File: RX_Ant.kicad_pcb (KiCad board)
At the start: 2 copper layers, 100 x 100 mm, 44 parts, among them J1 CONN_COAXIAL, J10 CONN_COAXIAL, J11 CONN_01X06, J12 CONN_01X05, J13 CONN_COAXIAL, J14 CONN_COAXIAL, J15 CONN_COAXIAL, J16 CONN_01X01, J17 CONN_01X01, J18 CONN_01X01, J19 CONN_01X01, J2 CONN_COAXIAL, J20 CONN_01X01, J21 CONN_01X01, J22 CONN_01X01, J23 CONN_01X01, J3 CONN_COAXIAL, J4 CONN_COAXIAL, J5 CONN_COAXIAL, J6 CONN_COAXIAL, J7 CONN_COAXIAL, J8 CONN_COAXIAL, J9 CONN_COAXIAL

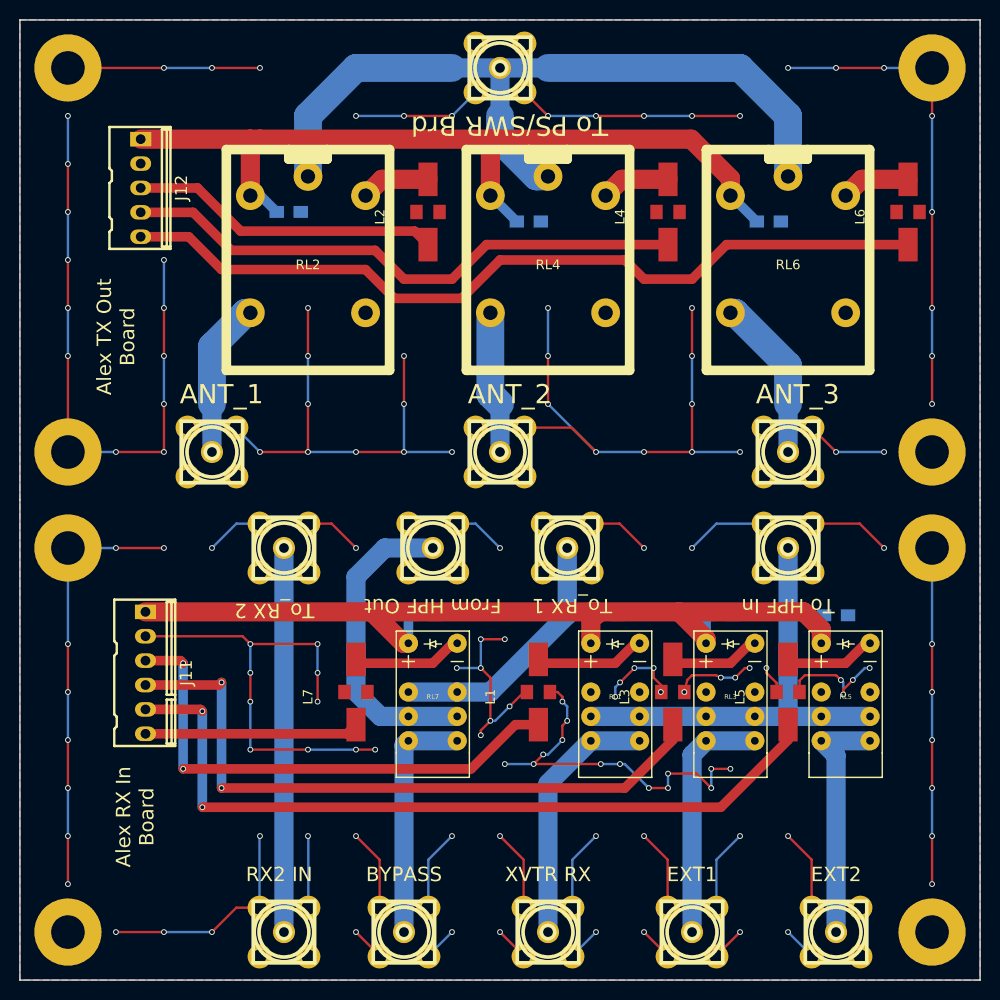
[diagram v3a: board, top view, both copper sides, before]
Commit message: few more vias added, tidying up some silkmask
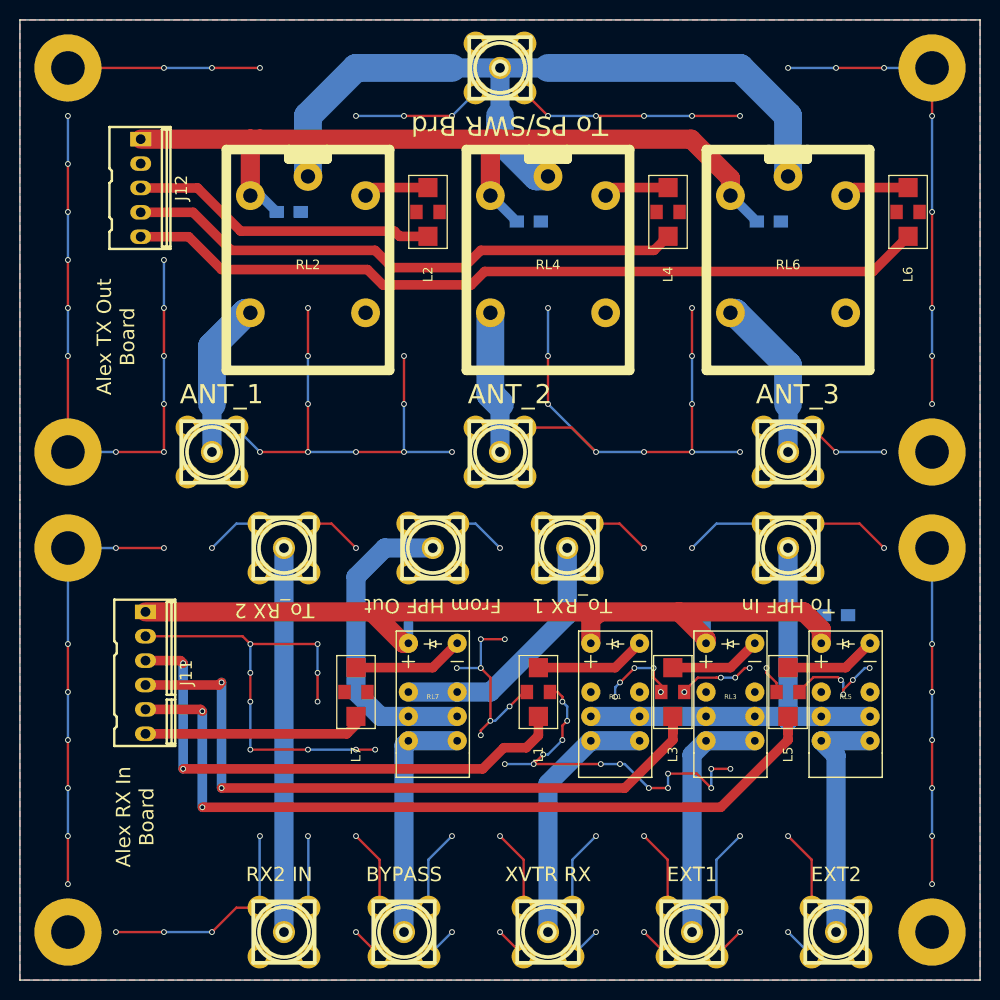
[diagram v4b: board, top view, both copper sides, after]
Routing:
- net Ant_3: track 86.6 -> 84.1 mm
- net RX3_IN: track 81.5 -> 83.2 mm
- net RX2_IN: track 69.7 -> 71.4 mm
- net Xvtr_IN: track 53.9 -> 55.5 mm
- net GND: track 661.1 -> 659.7 mm
- net Ant_2: track 59.3 -> 58.7 mm

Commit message: Gerber and BOM files added
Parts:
- added J24: CONN_COAXIAL, Connector_Coaxial:SMA_Amphenol_132289_EdgeMount, F.Cu at (47.4, 77.6)
- added J25: CONN_COAXIAL, Connector_Coaxial:SMA_Amphenol_132289_EdgeMount, F.Cu at (40.0, 72.4)
- added J26: CONN_COAXIAL, Connector_Coaxial:SMA_Amphenol_132289_EdgeMount, F.Cu at (75.0, 122.4)
- added J27: CONN_COAXIAL, Connector_Coaxial:SMA_Amphenol_132289_EdgeMount, F.Cu at (70.0, 72.4)
- added J28: CONN_COAXIAL, Connector_Coaxial:SMA_Amphenol_132289_EdgeMount, F.Cu at (100.0, 77.6)
- added J29: CONN_COAXIAL, Connector_Coaxial:SMA_Amphenol_132289_EdgeMount, F.Cu at (90.0, 122.4)
- added J30: CONN_COAXIAL, Connector_Coaxial:SMA_Amphenol_132289_EdgeMount, F.Cu at (100.0, 72.4)
- added J31: CONN_COAXIAL, Connector_Coaxial:SMA_Amphenol_132289_EdgeMount, F.Cu at (105.0, 122.4)
- added J32: CONN_COAXIAL, Connector_Coaxial:SMA_Amphenol_132289_EdgeMount, F.Cu at (60.0, 122.4)
- added J33: CONN_COAXIAL, Connector_Coaxial:SMA_Amphenol_132289_EdgeMount, F.Cu at (45.0, 122.4)
- added J34: CONN_COAXIAL, Connector_Coaxial:SMA_Amphenol_132289_EdgeMount, F.Cu at (70.0, 27.6)
- added J35: CONN_COAXIAL, Connector_Coaxial:SMA_Amphenol_132289_EdgeMount, F.Cu at (63.0, 77.6)
- added J36: CONN_COAXIAL, Connector_Coaxial:SMA_Amphenol_132289_EdgeMount, F.Cu at (78.0, 77.6)
- moved C9 5.23 mm to (62.6, 92.2)
- moved J13 2.50 mm to (45.0, 120.0)
- moved C5 2.00 mm to (83.0, 87.0)
- moved J7 1.00 mm to (78.0, 80.0)
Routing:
- net GND: track 659.7 -> 1060.8 mm, vias 137 -> 171
- net Net-(J34-Pad1): track 80.8 -> 71.0 mm
- net Net-(J13-Pad1): track 40.0 -> 45.9 mm
- net Net-(J36-Pad1): track 26.9 -> 29.7 mm
- net +12V: track 189.0 -> 186.4 mm
- net Net-(J32-Pad1): track 25.2 -> 27.6 mm
- net Net-(J31-Pad1): track 25.6 -> 28.0 mm
- net Net-(J29-Pad1): track 25.6 -> 28.0 mm
- net Net-(J28-Pad1): track 47.5 -> 49.9 mm
- net Net-(J27-Pad1): track 14.9 -> 17.3 mm
- net Net-(J2-Pad1): track 16.4 -> 18.8 mm
- net Net-(J10-Pad1): track 17.3 -> 19.7 mm
- net Net-(J1-Pad1): track 26.8 -> 29.2 mm
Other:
- board text added: "Ἀλεξιάρης"

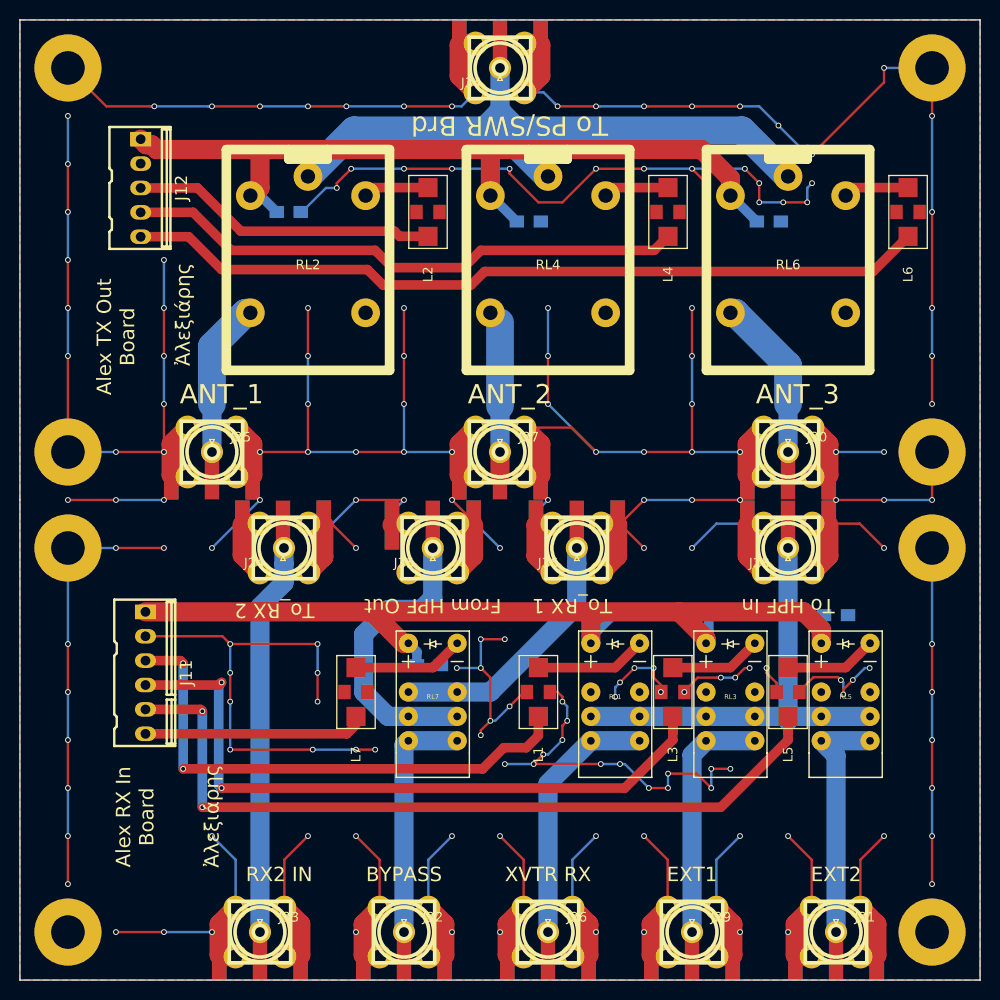
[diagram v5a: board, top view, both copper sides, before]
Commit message: via stitching added, new gerber
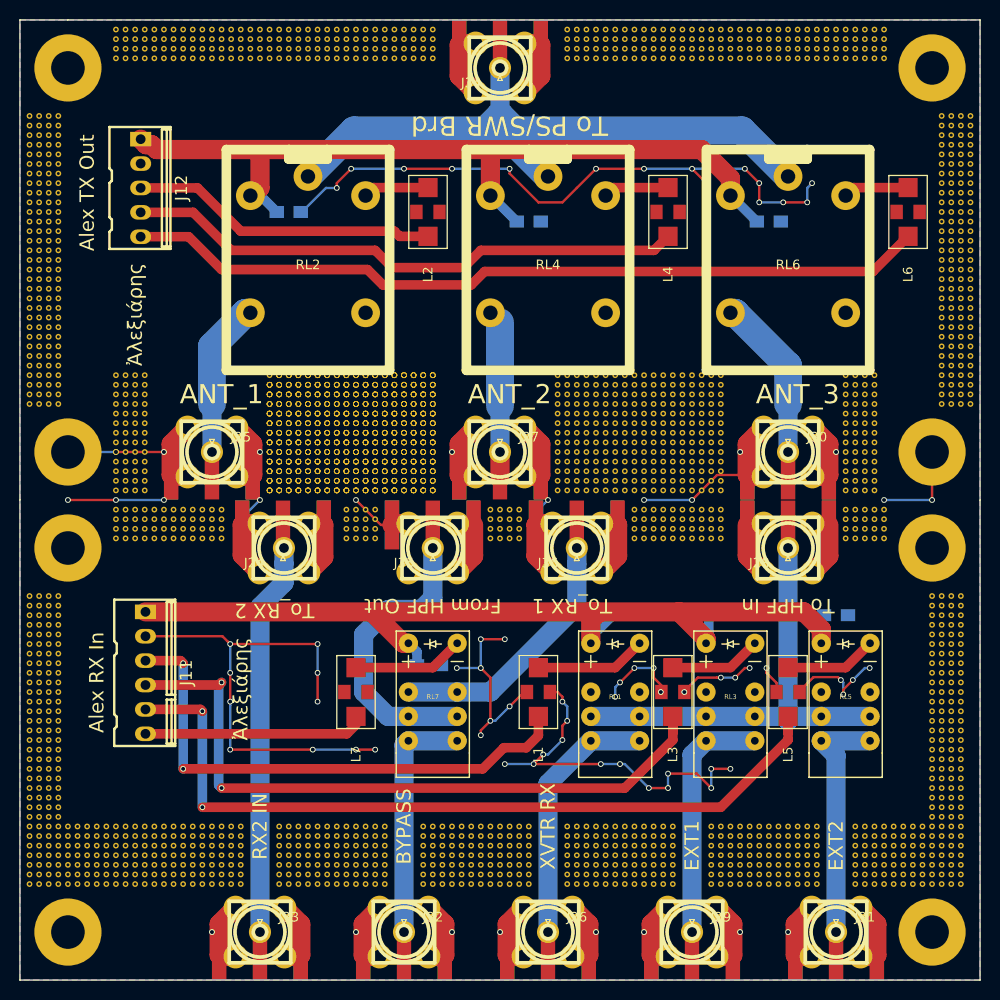
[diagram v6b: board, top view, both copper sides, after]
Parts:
- added REF**: via, via:via, F.Cu at (33.0, 74.0)
- added REF**: via, via:via, F.Cu at (32.0, 72.0)
- added REF**: via, via:via, F.Cu at (85.0, 77.0)
- added REF** (x3): via, via:via, F.Cu at (59.0, 71.0)
- added REF** (x3): via, via:via, F.Cu at (58.0, 71.0)
- added REF** (x3): via, via:via, F.Cu at (57.0, 71.0)
- added REF** (x3): via, via:via, F.Cu at (56.0, 71.0)
- added REF** (x3): via, via:via, F.Cu at (55.0, 71.0)
- added REF** (x3): via, via:via, F.Cu at (54.0, 71.0)
- added REF** (x3): via, via:via, F.Cu at (53.0, 71.0)
- added REF** (x3): via, via:via, F.Cu at (52.0, 71.0)
- added REF** (x3): via, via:via, F.Cu at (51.0, 71.0)
- added REF** (x3): via, via:via, F.Cu at (50.0, 71.0)
- added REF**: via, via:via, F.Cu at (84.0, 77.0)
- added REF** (x3): via, via:via, F.Cu at (49.0, 71.0)
- added REF** (x3): via, via:via, F.Cu at (48.0, 71.0)
- added REF** (x3): via, via:via, F.Cu at (47.0, 71.0)
- added REF** (x3): via, via:via, F.Cu at (46.0, 71.0)
- added REF** (x3): via, via:via, F.Cu at (63.0, 70.0)
- added REF** (x3): via, via:via, F.Cu at (62.0, 70.0)
- added REF** (x3): via, via:via, F.Cu at (61.0, 70.0)
- added REF** (x3): via, via:via, F.Cu at (60.0, 70.0)
- added REF** (x3): via, via:via, F.Cu at (59.0, 70.0)
- added REF** (x3): via, via:via, F.Cu at (58.0, 70.0)
- added REF**: via, via:via, F.Cu at (93.0, 76.0)
- added REF** (x3): via, via:via, F.Cu at (57.0, 70.0)
- added REF** (x3): via, via:via, F.Cu at (56.0, 70.0)
- added REF** (x3): via, via:via, F.Cu at (55.0, 70.0)
- added REF** (x3): via, via:via, F.Cu at (54.0, 70.0)
- added REF** (x3): via, via:via, F.Cu at (53.0, 70.0)
- added REF** (x3): via, via:via, F.Cu at (52.0, 70.0)
- added REF** (x3): via, via:via, F.Cu at (51.0, 70.0)
- added REF** (x3): via, via:via, F.Cu at (50.0, 70.0)
- added REF** (x3): via, via:via, F.Cu at (49.0, 70.0)
- added REF** (x3): via, via:via, F.Cu at (48.0, 70.0)
- added REF**: via, via:via, F.Cu at (92.0, 76.0)
- added REF** (x3): via, via:via, F.Cu at (47.0, 70.0)
- added REF** (x3): via, via:via, F.Cu at (46.0, 70.0)
- added REF** (x3): via, via:via, F.Cu at (63.0, 69.0)
- added REF** (x3): via, via:via, F.Cu at (62.0, 69.0)
- added REF** (x3): via, via:via, F.Cu at (61.0, 69.0)
- added REF** (x3): via, via:via, F.Cu at (60.0, 69.0)
- added REF** (x3): via, via:via, F.Cu at (59.0, 69.0)
- added REF** (x3): via, via:via, F.Cu at (58.0, 69.0)
- added REF** (x3): via, via:via, F.Cu at (57.0, 69.0)
- added REF** (x3): via, via:via, F.Cu at (56.0, 69.0)
- added REF**: via, via:via, F.Cu at (91.0, 76.0)
- added REF** (x3): via, via:via, F.Cu at (55.0, 69.0)
- added REF** (x3): via, via:via, F.Cu at (54.0, 69.0)
- added REF** (x3): via, via:via, F.Cu at (53.0, 69.0)
- added REF** (x3): via, via:via, F.Cu at (52.0, 69.0)
- added REF** (x3): via, via:via, F.Cu at (51.0, 69.0)
- added REF** (x3): via, via:via, F.Cu at (50.0, 69.0)
- added REF** (x3): via, via:via, F.Cu at (49.0, 69.0)
- added REF** (x3): via, via:via, F.Cu at (48.0, 69.0)
- added REF** (x3): via, via:via, F.Cu at (47.0, 69.0)
- added REF** (x3): via, via:via, F.Cu at (46.0, 69.0)
- added REF**: via, via:via, F.Cu at (90.0, 76.0)
- added REF** (x3): via, via:via, F.Cu at (63.0, 68.0)
- added REF** (x3): via, via:via, F.Cu at (62.0, 68.0)
- added REF** (x3): via, via:via, F.Cu at (61.0, 68.0)
- added REF** (x3): via, via:via, F.Cu at (60.0, 68.0)
- added REF** (x3): via, via:via, F.Cu at (59.0, 68.0)
- added REF** (x3): via, via:via, F.Cu at (58.0, 68.0)
- added REF** (x3): via, via:via, F.Cu at (57.0, 68.0)
- added REF** (x3): via, via:via, F.Cu at (56.0, 68.0)
- added REF** (x3): via, via:via, F.Cu at (55.0, 68.0)
- added REF** (x3): via, via:via, F.Cu at (54.0, 68.0)
- added REF**: via, via:via, F.Cu at (89.0, 76.0)
- added REF** (x3): via, via:via, F.Cu at (53.0, 68.0)
- added REF** (x3): via, via:via, F.Cu at (52.0, 68.0)
- added REF** (x3): via, via:via, F.Cu at (51.0, 68.0)
- added REF** (x3): via, via:via, F.Cu at (50.0, 68.0)
- added REF** (x3): via, via:via, F.Cu at (49.0, 68.0)
- added REF** (x3): via, via:via, F.Cu at (48.0, 68.0)
- added REF** (x3): via, via:via, F.Cu at (47.0, 68.0)
- added REF** (x3): via, via:via, F.Cu at (46.0, 68.0)
- added REF** (x3): via, via:via, F.Cu at (63.0, 67.0)
- added REF** (x3): via, via:via, F.Cu at (62.0, 67.0)
- added REF**: via, via:via, F.Cu at (88.0, 76.0)
- added REF** (x3): via, via:via, F.Cu at (61.0, 67.0)
- added REF** (x3): via, via:via, F.Cu at (60.0, 67.0)
- added REF** (x3): via, via:via, F.Cu at (59.0, 67.0)
- added REF** (x3): via, via:via, F.Cu at (58.0, 67.0)
- added REF** (x3): via, via:via, F.Cu at (57.0, 67.0)
- added REF** (x3): via, via:via, F.Cu at (56.0, 67.0)
- added REF** (x3): via, via:via, F.Cu at (55.0, 67.0)
- added REF** (x3): via, via:via, F.Cu at (54.0, 67.0)
- added REF** (x3): via, via:via, F.Cu at (53.0, 67.0)
- added REF** (x3): via, via:via, F.Cu at (52.0, 67.0)
- added REF**: via, via:via, F.Cu at (87.0, 76.0)
- added REF** (x3): via, via:via, F.Cu at (51.0, 67.0)
- added REF** (x3): via, via:via, F.Cu at (50.0, 67.0)
- added REF** (x3): via, via:via, F.Cu at (49.0, 67.0)
- added REF** (x3): via, via:via, F.Cu at (48.0, 67.0)
- added REF** (x3): via, via:via, F.Cu at (47.0, 67.0)
- added REF** (x3): via, via:via, F.Cu at (46.0, 67.0)
- added REF** (x3): via, via:via, F.Cu at (63.0, 66.0)
- added REF** (x3): via, via:via, F.Cu at (62.0, 66.0)
- added REF** (x3): via, via:via, F.Cu at (61.0, 66.0)
- added REF** (x3): via, via:via, F.Cu at (60.0, 66.0)
- added REF**: via, via:via, F.Cu at (86.0, 76.0)
- added REF** (x3): via, via:via, F.Cu at (59.0, 66.0)
- added REF** (x3): via, via:via, F.Cu at (58.0, 66.0)
- added REF** (x3): via, via:via, F.Cu at (57.0, 66.0)
- added REF** (x3): via, via:via, F.Cu at (56.0, 66.0)
- added REF** (x3): via, via:via, F.Cu at (55.0, 66.0)
- added REF** (x3): via, via:via, F.Cu at (54.0, 66.0)
- added REF** (x3): via, via:via, F.Cu at (53.0, 66.0)
- added REF** (x3): via, via:via, F.Cu at (52.0, 66.0)
- added REF** (x3): via, via:via, F.Cu at (51.0, 66.0)
- added REF** (x3): via, via:via, F.Cu at (50.0, 66.0)
- added REF**: via, via:via, F.Cu at (31.0, 72.0)
- added REF**: via, via:via, F.Cu at (85.0, 76.0)
- added REF** (x3): via, via:via, F.Cu at (49.0, 66.0)
- added REF** (x3): via, via:via, F.Cu at (48.0, 66.0)
- added REF** (x3): via, via:via, F.Cu at (47.0, 66.0)
- added REF** (x3): via, via:via, F.Cu at (46.0, 66.0)
- added REF** (x3): via, via:via, F.Cu at (63.0, 65.0)
- added REF** (x3): via, via:via, F.Cu at (62.0, 65.0)
- added REF** (x3): via, via:via, F.Cu at (61.0, 65.0)
- added REF** (x3): via, via:via, F.Cu at (60.0, 65.0)
- added REF** (x3): via, via:via, F.Cu at (59.0, 65.0)
- added REF** (x3): via, via:via, F.Cu at (58.0, 65.0)
- added REF**: via, via:via, F.Cu at (84.0, 76.0)
- added REF** (x3): via, via:via, F.Cu at (57.0, 65.0)
- added REF** (x3): via, via:via, F.Cu at (56.0, 65.0)
- added REF** (x3): via, via:via, F.Cu at (55.0, 65.0)
- added REF** (x3): via, via:via, F.Cu at (54.0, 65.0)
- added REF** (x3): via, via:via, F.Cu at (53.0, 65.0)
- added REF** (x3): via, via:via, F.Cu at (52.0, 65.0)
- added REF** (x3): via, via:via, F.Cu at (51.0, 65.0)
- added REF** (x3): via, via:via, F.Cu at (50.0, 65.0)
- added REF** (x3): via, via:via, F.Cu at (49.0, 65.0)
- added REF** (x3): via, via:via, F.Cu at (48.0, 65.0)
- added REF**: via, via:via, F.Cu at (72.0, 79.0)
- added REF** (x3): via, via:via, F.Cu at (47.0, 65.0)
- added REF** (x3): via, via:via, F.Cu at (46.0, 65.0)
- added REF** (x3): via, via:via, F.Cu at (63.0, 64.0)
- added REF** (x3): via, via:via, F.Cu at (62.0, 64.0)
- added REF** (x3): via, via:via, F.Cu at (61.0, 64.0)
- added REF** (x3): via, via:via, F.Cu at (60.0, 64.0)
- added REF** (x3): via, via:via, F.Cu at (59.0, 64.0)
- added REF** (x3): via, via:via, F.Cu at (58.0, 64.0)
- added REF** (x3): via, via:via, F.Cu at (57.0, 64.0)
- added REF** (x3): via, via:via, F.Cu at (56.0, 64.0)
- added REF**: via, via:via, F.Cu at (71.0, 79.0)
- added REF** (x3): via, via:via, F.Cu at (55.0, 64.0)
- added REF** (x3): via, via:via, F.Cu at (54.0, 64.0)
- added REF** (x3): via, via:via, F.Cu at (53.0, 64.0)
- added REF** (x3): via, via:via, F.Cu at (52.0, 64.0)
- added REF** (x3): via, via:via, F.Cu at (51.0, 64.0)
- added REF** (x3): via, via:via, F.Cu at (50.0, 64.0)
- added REF** (x3): via, via:via, F.Cu at (49.0, 64.0)
- added REF** (x3): via, via:via, F.Cu at (48.0, 64.0)
- added REF** (x3): via, via:via, F.Cu at (47.0, 64.0)
- added REF** (x3): via, via:via, F.Cu at (46.0, 64.0)
- added REF**: via, via:via, F.Cu at (70.0, 79.0)
- added REF** (x3): via, via:via, F.Cu at (63.0, 63.0)
- added REF** (x3): via, via:via, F.Cu at (62.0, 63.0)
- added REF** (x3): via, via:via, F.Cu at (61.0, 63.0)
- added REF** (x3): via, via:via, F.Cu at (60.0, 63.0)
- added REF** (x3): via, via:via, F.Cu at (59.0, 63.0)
- added REF** (x3): via, via:via, F.Cu at (58.0, 63.0)
- added REF** (x3): via, via:via, F.Cu at (57.0, 63.0)
- added REF** (x3): via, via:via, F.Cu at (56.0, 63.0)
- added REF** (x3): via, via:via, F.Cu at (55.0, 63.0)
- added REF** (x3): via, via:via, F.Cu at (54.0, 63.0)
- added REF**: via, via:via, F.Cu at (69.0, 79.0)
- added REF** (x3): via, via:via, F.Cu at (53.0, 63.0)
- added REF** (x3): via, via:via, F.Cu at (52.0, 63.0)
- added REF** (x3): via, via:via, F.Cu at (51.0, 63.0)
- added REF** (x3): via, via:via, F.Cu at (50.0, 63.0)
- added REF** (x3): via, via:via, F.Cu at (49.0, 63.0)
- added REF** (x3): via, via:via, F.Cu at (48.0, 63.0)
- added REF** (x3): via, via:via, F.Cu at (47.0, 63.0)
- added REF** (x3): via, via:via, F.Cu at (46.0, 63.0)
- added REF** (x3): via, via:via, F.Cu at (63.0, 62.0)
- added REF** (x3): via, via:via, F.Cu at (62.0, 62.0)
- added REF**: via, via:via, F.Cu at (72.0, 78.0)
- added REF** (x3): via, via:via, F.Cu at (61.0, 62.0)
- added REF** (x3): via, via:via, F.Cu at (60.0, 62.0)
- added REF** (x3): via, via:via, F.Cu at (59.0, 62.0)
- added REF** (x3): via, via:via, F.Cu at (58.0, 62.0)
- added REF** (x3): via, via:via, F.Cu at (57.0, 62.0)
- added REF** (x3): via, via:via, F.Cu at (56.0, 62.0)
- added REF** (x3): via, via:via, F.Cu at (55.0, 62.0)
- added REF** (x3): via, via:via, F.Cu at (54.0, 62.0)
- added REF** (x3): via, via:via, F.Cu at (53.0, 62.0)
- added REF** (x3): via, via:via, F.Cu at (52.0, 62.0)
- added REF**: via, via:via, F.Cu at (71.0, 78.0)
- added REF** (x3): via, via:via, F.Cu at (51.0, 62.0)
- added REF** (x3): via, via:via, F.Cu at (50.0, 62.0)
- added REF** (x3): via, via:via, F.Cu at (49.0, 62.0)
- added REF** (x3): via, via:via, F.Cu at (48.0, 62.0)
- added REF** (x3): via, via:via, F.Cu at (47.0, 62.0)
- added REF**: via, via:via, F.Cu at (76.0, 62.0)
- added REF**: via, via:via, F.Cu at (46.0, 62.0)
- added REF**: via, via:via, F.Cu at (30.0, 62.0)
- added REF**: via, via:via, F.Cu at (114.0, 115.0)
- added REF**: via, via:via, F.Cu at (113.0, 115.0)
- added REF**: via, via:via, F.Cu at (70.0, 78.0)
- added REF**: via, via:via, F.Cu at (112.0, 115.0)
- added REF**: via, via:via, F.Cu at (111.0, 115.0)
- added REF**: via, via:via, F.Cu at (110.0, 115.0)
- added REF**: via, via:via, F.Cu at (109.0, 115.0)
- added REF**: via, via:via, F.Cu at (108.0, 115.0)
- added REF**: via, via:via, F.Cu at (107.0, 115.0)
- added REF**: via, via:via, F.Cu at (114.0, 114.0)
- added REF**: via, via:via, F.Cu at (113.0, 114.0)
- added REF**: via, via:via, F.Cu at (112.0, 114.0)
- added REF**: via, via:via, F.Cu at (111.0, 114.0)
- added REF**: via, via:via, F.Cu at (69.0, 78.0)
- added REF**: via, via:via, F.Cu at (110.0, 114.0)
- added REF**: via, via:via, F.Cu at (109.0, 114.0)
- added REF**: via, via:via, F.Cu at (108.0, 114.0)
- added REF**: via, via:via, F.Cu at (107.0, 114.0)
- added REF**: via, via:via, F.Cu at (114.0, 113.0)
- added REF**: via, via:via, F.Cu at (113.0, 113.0)
- added REF**: via, via:via, F.Cu at (112.0, 113.0)
- added REF**: via, via:via, F.Cu at (111.0, 113.0)
- added REF**: via, via:via, F.Cu at (110.0, 113.0)
- added REF**: via, via:via, F.Cu at (109.0, 113.0)
- added REF**: via, via:via, F.Cu at (30.0, 72.0)
- added REF**: via, via:via, F.Cu at (72.0, 77.0)
- added REF**: via, via:via, F.Cu at (108.0, 113.0)
- added REF**: via, via:via, F.Cu at (107.0, 113.0)
- added REF**: via, via:via, F.Cu at (114.0, 112.0)
- added REF**: via, via:via, F.Cu at (113.0, 112.0)
- added REF**: via, via:via, F.Cu at (112.0, 112.0)
- added REF**: via, via:via, F.Cu at (111.0, 112.0)
- added REF**: via, via:via, F.Cu at (110.0, 112.0)
- added REF**: via, via:via, F.Cu at (109.0, 112.0)
- added REF**: via, via:via, F.Cu at (108.0, 112.0)
- added REF**: via, via:via, F.Cu at (107.0, 112.0)
- added REF**: via, via:via, F.Cu at (71.0, 77.0)
- added REF**: via, via:via, F.Cu at (114.0, 111.0)
- added REF**: via, via:via, F.Cu at (113.0, 111.0)
- added REF**: via, via:via, F.Cu at (112.0, 111.0)
- added REF**: via, via:via, F.Cu at (111.0, 111.0)
- added REF**: via, via:via, F.Cu at (110.0, 111.0)
- added REF**: via, via:via, F.Cu at (109.0, 111.0)
- added REF**: via, via:via, F.Cu at (108.0, 111.0)
- added REF**: via, via:via, F.Cu at (107.0, 111.0)
- added REF**: via, via:via, F.Cu at (114.0, 110.0)
- added REF**: via, via:via, F.Cu at (113.0, 110.0)
- added REF**: via, via:via, F.Cu at (70.0, 77.0)
- added REF**: via, via:via, F.Cu at (112.0, 110.0)
- added REF**: via, via:via, F.Cu at (111.0, 110.0)
- added REF**: via, via:via, F.Cu at (110.0, 110.0)
- added REF**: via, via:via, F.Cu at (109.0, 110.0)
- added REF**: via, via:via, F.Cu at (108.0, 110.0)
- added REF**: via, via:via, F.Cu at (107.0, 110.0)
- added REF**: via, via:via, F.Cu at (114.0, 109.0)
- added REF**: via, via:via, F.Cu at (113.0, 109.0)
- added REF**: via, via:via, F.Cu at (112.0, 109.0)
- added REF**: via, via:via, F.Cu at (111.0, 109.0)
- added REF**: via, via:via, F.Cu at (69.0, 77.0)
- added REF**: via, via:via, F.Cu at (110.0, 109.0)
- added REF**: via, via:via, F.Cu at (109.0, 109.0)
- added REF**: via, via:via, F.Cu at (108.0, 109.0)
- added REF**: via, via:via, F.Cu at (43.0, 115.0)
- added REF**: via, via:via, F.Cu at (42.0, 115.0)
- added REF**: via, via:via, F.Cu at (41.0, 115.0)
- added REF**: via, via:via, F.Cu at (40.0, 115.0)
- added REF**: via, via:via, F.Cu at (39.0, 115.0)
- added REF**: via, via:via, F.Cu at (38.0, 115.0)
- added REF**: via, via:via, F.Cu at (37.0, 115.0)
- added REF**: via, via:via, F.Cu at (72.0, 76.0)
- added REF**: via, via:via, F.Cu at (36.0, 115.0)
- added REF**: via, via:via, F.Cu at (35.0, 115.0)
- added REF**: via, via:via, F.Cu at (34.0, 115.0)
- added REF**: via, via:via, F.Cu at (33.0, 115.0)
- added REF**: via, via:via, F.Cu at (32.0, 115.0)
- added REF**: via, via:via, F.Cu at (31.0, 115.0)
- added REF**: via, via:via, F.Cu at (30.0, 115.0)
- added REF**: via, via:via, F.Cu at (29.0, 115.0)
- added REF**: via, via:via, F.Cu at (28.0, 115.0)
- added REF**: via, via:via, F.Cu at (27.0, 115.0)
- added REF**: via, via:via, F.Cu at (71.0, 76.0)
- added REF**: via, via:via, F.Cu at (26.0, 115.0)
- added REF**: via, via:via, F.Cu at (25.0, 115.0)
- added REF**: via, via:via, F.Cu at (43.0, 114.0)
- added REF**: via, via:via, F.Cu at (42.0, 114.0)
- added REF**: via, via:via, F.Cu at (41.0, 114.0)
- added REF**: via, via:via, F.Cu at (40.0, 114.0)
- added REF**: via, via:via, F.Cu at (39.0, 114.0)
- added REF**: via, via:via, F.Cu at (38.0, 114.0)
- added REF**: via, via:via, F.Cu at (37.0, 114.0)
- added REF**: via, via:via, F.Cu at (36.0, 114.0)
- added REF**: via, via:via, F.Cu at (70.0, 76.0)
- added REF**: via, via:via, F.Cu at (35.0, 114.0)
- added REF**: via, via:via, F.Cu at (34.0, 114.0)
- added REF**: via, via:via, F.Cu at (33.0, 114.0)
- added REF**: via, via:via, F.Cu at (32.0, 114.0)
- added REF**: via, via:via, F.Cu at (31.0, 114.0)
- added REF**: via, via:via, F.Cu at (30.0, 114.0)
- added REF**: via, via:via, F.Cu at (29.0, 114.0)
- added REF**: via, via:via, F.Cu at (28.0, 114.0)
- added REF**: via, via:via, F.Cu at (27.0, 114.0)
- added REF**: via, via:via, F.Cu at (26.0, 114.0)
- added REF**: via, via:via, F.Cu at (69.0, 76.0)
- added REF**: via, via:via, F.Cu at (25.0, 114.0)
- added REF**: via, via:via, F.Cu at (43.0, 113.0)
- added REF**: via, via:via, F.Cu at (42.0, 113.0)
- added REF**: via, via:via, F.Cu at (41.0, 113.0)
- added REF**: via, via:via, F.Cu at (40.0, 113.0)
- added REF**: via, via:via, F.Cu at (39.0, 113.0)
- added REF**: via, via:via, F.Cu at (38.0, 113.0)
- added REF**: via, via:via, F.Cu at (37.0, 113.0)
- added REF**: via, via:via, F.Cu at (36.0, 113.0)
- added REF**: via, via:via, F.Cu at (35.0, 113.0)
- added REF**: via, via:via, F.Cu at (57.0, 79.0)
- added REF**: via, via:via, F.Cu at (34.0, 113.0)
- added REF**: via, via:via, F.Cu at (33.0, 113.0)
- added REF**: via, via:via, F.Cu at (32.0, 113.0)
- added REF**: via, via:via, F.Cu at (31.0, 113.0)
- added REF**: via, via:via, F.Cu at (30.0, 113.0)
- added REF**: via, via:via, F.Cu at (29.0, 113.0)
- added REF**: via, via:via, F.Cu at (28.0, 113.0)
- added REF**: via, via:via, F.Cu at (27.0, 113.0)
- added REF**: via, via:via, F.Cu at (26.0, 113.0)
- added REF**: via, via:via, F.Cu at (25.0, 113.0)
- added REF**: via, via:via, F.Cu at (56.0, 79.0)
- added REF**: via, via:via, F.Cu at (43.0, 112.0)
- added REF**: via, via:via, F.Cu at (42.0, 112.0)
- added REF**: via, via:via, F.Cu at (41.0, 112.0)
- added REF**: via, via:via, F.Cu at (40.0, 112.0)
- added REF**: via, via:via, F.Cu at (39.0, 112.0)
- added REF**: via, via:via, F.Cu at (38.0, 112.0)
- added REF**: via, via:via, F.Cu at (37.0, 112.0)
- added REF**: via, via:via, F.Cu at (36.0, 112.0)
- added REF**: via, via:via, F.Cu at (35.0, 112.0)
- added REF**: via, via:via, F.Cu at (34.0, 112.0)
- added REF**: via, via:via, F.Cu at (33.0, 71.0)
- added REF**: via, via:via, F.Cu at (55.0, 79.0)
- added REF**: via, via:via, F.Cu at (33.0, 112.0)
- added REF**: via, via:via, F.Cu at (32.0, 112.0)
- added REF**: via, via:via, F.Cu at (31.0, 112.0)
- added REF**: via, via:via, F.Cu at (30.0, 112.0)
- added REF**: via, via:via, F.Cu at (29.0, 112.0)
- added REF**: via, via:via, F.Cu at (28.0, 112.0)
- added REF**: via, via:via, F.Cu at (27.0, 112.0)
- added REF**: via, via:via, F.Cu at (26.0, 112.0)
- added REF**: via, via:via, F.Cu at (25.0, 112.0)
- added REF**: via, via:via, F.Cu at (43.0, 111.0)
- added REF**: via, via:via, F.Cu at (54.0, 79.0)
- added REF**: via, via:via, F.Cu at (42.0, 111.0)
- added REF**: via, via:via, F.Cu at (41.0, 111.0)
- added REF**: via, via:via, F.Cu at (40.0, 111.0)
- added REF**: via, via:via, F.Cu at (39.0, 111.0)
- added REF**: via, via:via, F.Cu at (38.0, 111.0)
- added REF**: via, via:via, F.Cu at (37.0, 111.0)
- added REF**: via, via:via, F.Cu at (36.0, 111.0)
- added REF**: via, via:via, F.Cu at (35.0, 111.0)
- added REF**: via, via:via, F.Cu at (34.0, 111.0)
- added REF**: via, via:via, F.Cu at (33.0, 111.0)
- added REF**: via, via:via, F.Cu at (57.0, 78.0)
- added REF**: via, via:via, F.Cu at (32.0, 111.0)
- added REF**: via, via:via, F.Cu at (31.0, 111.0)
- added REF**: via, via:via, F.Cu at (30.0, 111.0)
- added REF**: via, via:via, F.Cu at (29.0, 111.0)
- added REF**: via, via:via, F.Cu at (28.0, 111.0)
- added REF**: via, via:via, F.Cu at (27.0, 111.0)
- added REF**: via, via:via, F.Cu at (26.0, 111.0)
- added REF**: via, via:via, F.Cu at (25.0, 111.0)
- added REF**: via, via:via, F.Cu at (43.0, 110.0)
- added REF**: via, via:via, F.Cu at (42.0, 110.0)
- added REF**: via, via:via, F.Cu at (56.0, 78.0)
- added REF**: via, via:via, F.Cu at (41.0, 110.0)
- added REF**: via, via:via, F.Cu at (40.0, 110.0)
- added REF**: via, via:via, F.Cu at (39.0, 110.0)
- added REF**: via, via:via, F.Cu at (38.0, 110.0)
- added REF**: via, via:via, F.Cu at (37.0, 110.0)
- added REF**: via, via:via, F.Cu at (36.0, 110.0)
- added REF**: via, via:via, F.Cu at (35.0, 110.0)
- added REF**: via, via:via, F.Cu at (34.0, 110.0)
- added REF**: via, via:via, F.Cu at (33.0, 110.0)
- added REF**: via, via:via, F.Cu at (32.0, 110.0)
- added REF**: via, via:via, F.Cu at (55.0, 78.0)
- added REF**: via, via:via, F.Cu at (31.0, 110.0)
- added REF**: via, via:via, F.Cu at (30.0, 110.0)
- added REF**: via, via:via, F.Cu at (29.0, 110.0)
- added REF**: via, via:via, F.Cu at (28.0, 110.0)
- added REF**: via, via:via, F.Cu at (27.0, 110.0)
- added REF**: via, via:via, F.Cu at (26.0, 110.0)
- added REF**: via, via:via, F.Cu at (25.0, 110.0)
- added REF**: via, via:via, F.Cu at (43.0, 109.0)
- added REF**: via, via:via, F.Cu at (42.0, 109.0)
- added REF**: via, via:via, F.Cu at (41.0, 109.0)
- added REF**: via, via:via, F.Cu at (54.0, 78.0)
- added REF**: via, via:via, F.Cu at (40.0, 109.0)
- added REF**: via, via:via, F.Cu at (39.0, 109.0)
- added REF**: via, via:via, F.Cu at (38.0, 109.0)
- added REF**: via, via:via, F.Cu at (37.0, 109.0)
- added REF**: via, via:via, F.Cu at (36.0, 109.0)
- added REF**: via, via:via, F.Cu at (35.0, 109.0)
- added REF**: via, via:via, F.Cu at (34.0, 109.0)
- added REF**: via, via:via, F.Cu at (33.0, 109.0)
- added REF**: via, via:via, F.Cu at (32.0, 109.0)
- added REF**: via, via:via, F.Cu at (31.0, 109.0)
- added REF**: via, via:via, F.Cu at (57.0, 77.0)
- added REF**: via, via:via, F.Cu at (30.0, 109.0)
- added REF**: via, via:via, F.Cu at (29.0, 109.0)
- added REF**: via, via:via, F.Cu at (28.0, 109.0)
- added REF**: via, via:via, F.Cu at (27.0, 109.0)
- added REF**: via, via:via, F.Cu at (26.0, 109.0)
- added REF**: via, via:via, F.Cu at (58.0, 115.0)
- added REF**: via, via:via, F.Cu at (57.0, 115.0)
- added REF**: via, via:via, F.Cu at (56.0, 115.0)
- added REF**: via, via:via, F.Cu at (55.0, 115.0)
- added REF**: via, via:via, F.Cu at (54.0, 115.0)
- added REF**: via, via:via, F.Cu at (56.0, 77.0)
- added REF**: via, via:via, F.Cu at (53.0, 115.0)
- added REF**: via, via:via, F.Cu at (52.0, 115.0)
- added REF**: via, via:via, F.Cu at (51.0, 115.0)
- added REF**: via, via:via, F.Cu at (50.0, 115.0)
- added REF**: via, via:via, F.Cu at (49.0, 115.0)
- added REF**: via, via:via, F.Cu at (48.0, 115.0)
- added REF**: via, via:via, F.Cu at (47.0, 115.0)
- added REF**: via, via:via, F.Cu at (58.0, 114.0)
- added REF**: via, via:via, F.Cu at (57.0, 114.0)
- added REF**: via, via:via, F.Cu at (56.0, 114.0)
- added REF**: via, via:via, F.Cu at (55.0, 77.0)
- added REF**: via, via:via, F.Cu at (55.0, 114.0)
- added REF**: via, via:via, F.Cu at (54.0, 114.0)
- added REF**: via, via:via, F.Cu at (53.0, 114.0)
- added REF**: via, via:via, F.Cu at (52.0, 114.0)
- added REF**: via, via:via, F.Cu at (51.0, 114.0)
- added REF**: via, via:via, F.Cu at (50.0, 114.0)
- added REF**: via, via:via, F.Cu at (49.0, 114.0)
- added REF**: via, via:via, F.Cu at (48.0, 114.0)
- added REF**: via, via:via, F.Cu at (47.0, 114.0)
- added REF**: via, via:via, F.Cu at (58.0, 113.0)
- added REF**: via, via:via, F.Cu at (54.0, 77.0)
- added REF**: via, via:via, F.Cu at (57.0, 113.0)
- added REF**: via, via:via, F.Cu at (56.0, 113.0)
- added REF**: via, via:via, F.Cu at (55.0, 113.0)
- added REF**: via, via:via, F.Cu at (54.0, 113.0)
- added REF**: via, via:via, F.Cu at (53.0, 113.0)
- added REF**: via, via:via, F.Cu at (52.0, 113.0)
- added REF**: via, via:via, F.Cu at (51.0, 113.0)
- added REF**: via, via:via, F.Cu at (50.0, 113.0)
- added REF**: via, via:via, F.Cu at (49.0, 113.0)
- added REF**: via, via:via, F.Cu at (48.0, 113.0)
- added REF**: via, via:via, F.Cu at (32.0, 71.0)
- added REF**: via, via:via, F.Cu at (57.0, 76.0)
- added REF**: via, via:via, F.Cu at (47.0, 113.0)
- added REF**: via, via:via, F.Cu at (58.0, 112.0)
- added REF**: via, via:via, F.Cu at (57.0, 112.0)
- added REF**: via, via:via, F.Cu at (56.0, 112.0)
- added REF**: via, via:via, F.Cu at (55.0, 112.0)
- added REF**: via, via:via, F.Cu at (54.0, 112.0)
- added REF**: via, via:via, F.Cu at (53.0, 112.0)
- added REF**: via, via:via, F.Cu at (52.0, 112.0)
- added REF**: via, via:via, F.Cu at (51.0, 112.0)
- added REF**: via, via:via, F.Cu at (50.0, 112.0)
- added REF**: via, via:via, F.Cu at (56.0, 76.0)
- added REF**: via, via:via, F.Cu at (49.0, 112.0)
- added REF**: via, via:via, F.Cu at (48.0, 112.0)
- added REF**: via, via:via, F.Cu at (47.0, 112.0)
- added REF**: via, via:via, F.Cu at (58.0, 111.0)
- added REF**: via, via:via, F.Cu at (57.0, 111.0)
- added REF**: via, via:via, F.Cu at (56.0, 111.0)
- added REF**: via, via:via, F.Cu at (55.0, 111.0)
- added REF**: via, via:via, F.Cu at (54.0, 111.0)
- added REF**: via, via:via, F.Cu at (53.0, 111.0)
- added REF**: via, via:via, F.Cu at (52.0, 111.0)
- added REF**: via, via:via, F.Cu at (55.0, 76.0)
- added REF**: via, via:via, F.Cu at (51.0, 111.0)
- added REF**: via, via:via, F.Cu at (50.0, 111.0)
- added REF**: via, via:via, F.Cu at (49.0, 111.0)
- added REF**: via, via:via, F.Cu at (48.0, 111.0)
- added REF**: via, via:via, F.Cu at (47.0, 111.0)
- added REF**: via, via:via, F.Cu at (58.0, 110.0)
- added REF**: via, via:via, F.Cu at (57.0, 110.0)
- added REF**: via, via:via, F.Cu at (56.0, 110.0)
- added REF**: via, via:via, F.Cu at (55.0, 110.0)
- added REF**: via, via:via, F.Cu at (54.0, 110.0)
- added REF**: via, via:via, F.Cu at (54.0, 76.0)
- added REF**: via, via:via, F.Cu at (53.0, 110.0)
- added REF**: via, via:via, F.Cu at (52.0, 110.0)
- added REF**: via, via:via, F.Cu at (51.0, 110.0)
- added REF**: via, via:via, F.Cu at (50.0, 110.0)
- added REF**: via, via:via, F.Cu at (49.0, 110.0)
- added REF**: via, via:via, F.Cu at (48.0, 110.0)
- added REF**: via, via:via, F.Cu at (47.0, 110.0)
- added REF**: via, via:via, F.Cu at (58.0, 109.0)
- added REF**: via, via:via, F.Cu at (57.0, 109.0)
- added REF**: via, via:via, F.Cu at (56.0, 109.0)
- added REF**: via, via:via, F.Cu at (41.0, 79.0)
- added REF**: via, via:via, F.Cu at (55.0, 109.0)
- added REF**: via, via:via, F.Cu at (54.0, 109.0)
- added REF**: via, via:via, F.Cu at (53.0, 109.0)
- added REF**: via, via:via, F.Cu at (52.0, 109.0)
- added REF**: via, via:via, F.Cu at (51.0, 109.0)
- added REF**: via, via:via, F.Cu at (50.0, 109.0)
- added REF**: via, via:via, F.Cu at (49.0, 109.0)
- added REF**: via, via:via, F.Cu at (48.0, 109.0)
- added REF**: via, via:via, F.Cu at (103.0, 115.0)
- added REF**: via, via:via, F.Cu at (102.0, 115.0)
- added REF**: via, via:via, F.Cu at (40.0, 79.0)
- added REF**: via, via:via, F.Cu at (101.0, 115.0)
- added REF**: via, via:via, F.Cu at (100.0, 115.0)
- added REF**: via, via:via, F.Cu at (99.0, 115.0)
- added REF**: via, via:via, F.Cu at (98.0, 115.0)
- added REF**: via, via:via, F.Cu at (97.0, 115.0)
- added REF**: via, via:via, F.Cu at (96.0, 115.0)
- added REF**: via, via:via, F.Cu at (95.0, 115.0)
- added REF**: via, via:via, F.Cu at (94.0, 115.0)
- added REF**: via, via:via, F.Cu at (93.0, 115.0)
- added REF**: via, via:via, F.Cu at (92.0, 115.0)
- added REF**: via, via:via, F.Cu at (39.0, 79.0)
- added REF**: via, via:via, F.Cu at (103.0, 114.0)
- added REF**: via, via:via, F.Cu at (102.0, 114.0)
- added REF**: via, via:via, F.Cu at (101.0, 114.0)
- added REF**: via, via:via, F.Cu at (100.0, 114.0)
- added REF**: via, via:via, F.Cu at (99.0, 114.0)
- added REF**: via, via:via, F.Cu at (98.0, 114.0)
- added REF**: via, via:via, F.Cu at (97.0, 114.0)
- added REF**: via, via:via, F.Cu at (96.0, 114.0)
- added REF**: via, via:via, F.Cu at (95.0, 114.0)
- added REF**: via, via:via, F.Cu at (94.0, 114.0)
- added REF**: via, via:via, F.Cu at (38.0, 79.0)
- added REF**: via, via:via, F.Cu at (93.0, 114.0)
- added REF**: via, via:via, F.Cu at (92.0, 114.0)
- added REF**: via, via:via, F.Cu at (103.0, 113.0)
- added REF**: via, via:via, F.Cu at (102.0, 113.0)
- added REF**: via, via:via, F.Cu at (101.0, 113.0)
- added REF**: via, via:via, F.Cu at (100.0, 113.0)
- added REF**: via, via:via, F.Cu at (99.0, 113.0)
- added REF**: via, via:via, F.Cu at (98.0, 113.0)
- added REF**: via, via:via, F.Cu at (97.0, 113.0)
- added REF**: via, via:via, F.Cu at (96.0, 113.0)
- added REF**: via, via:via, F.Cu at (37.0, 79.0)
- added REF**: via, via:via, F.Cu at (95.0, 113.0)
- added REF**: via, via:via, F.Cu at (94.0, 113.0)
- added REF**: via, via:via, F.Cu at (93.0, 113.0)
- added REF**: via, via:via, F.Cu at (92.0, 113.0)
- added REF**: via, via:via, F.Cu at (103.0, 112.0)
- added REF**: via, via:via, F.Cu at (102.0, 112.0)
- added REF**: via, via:via, F.Cu at (101.0, 112.0)
- added REF**: via, via:via, F.Cu at (100.0, 112.0)
- added REF**: via, via:via, F.Cu at (99.0, 112.0)
- added REF**: via, via:via, F.Cu at (98.0, 112.0)
- added REF**: via, via:via, F.Cu at (36.0, 79.0)
- added REF**: via, via:via, F.Cu at (97.0, 112.0)
- added REF**: via, via:via, F.Cu at (96.0, 112.0)
- added REF**: via, via:via, F.Cu at (95.0, 112.0)
- added REF**: via, via:via, F.Cu at (94.0, 112.0)
- added REF**: via, via:via, F.Cu at (93.0, 112.0)
- added REF**: via, via:via, F.Cu at (92.0, 112.0)
- added REF**: via, via:via, F.Cu at (103.0, 111.0)
- added REF**: via, via:via, F.Cu at (102.0, 111.0)
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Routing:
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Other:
- board text added: "Alex RX In"
- board text added: "Alex TX Out"
- board text removed: "Alex RX In Board"
- board text removed: "Alex TX Out Board"

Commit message: via stitching, gerber added
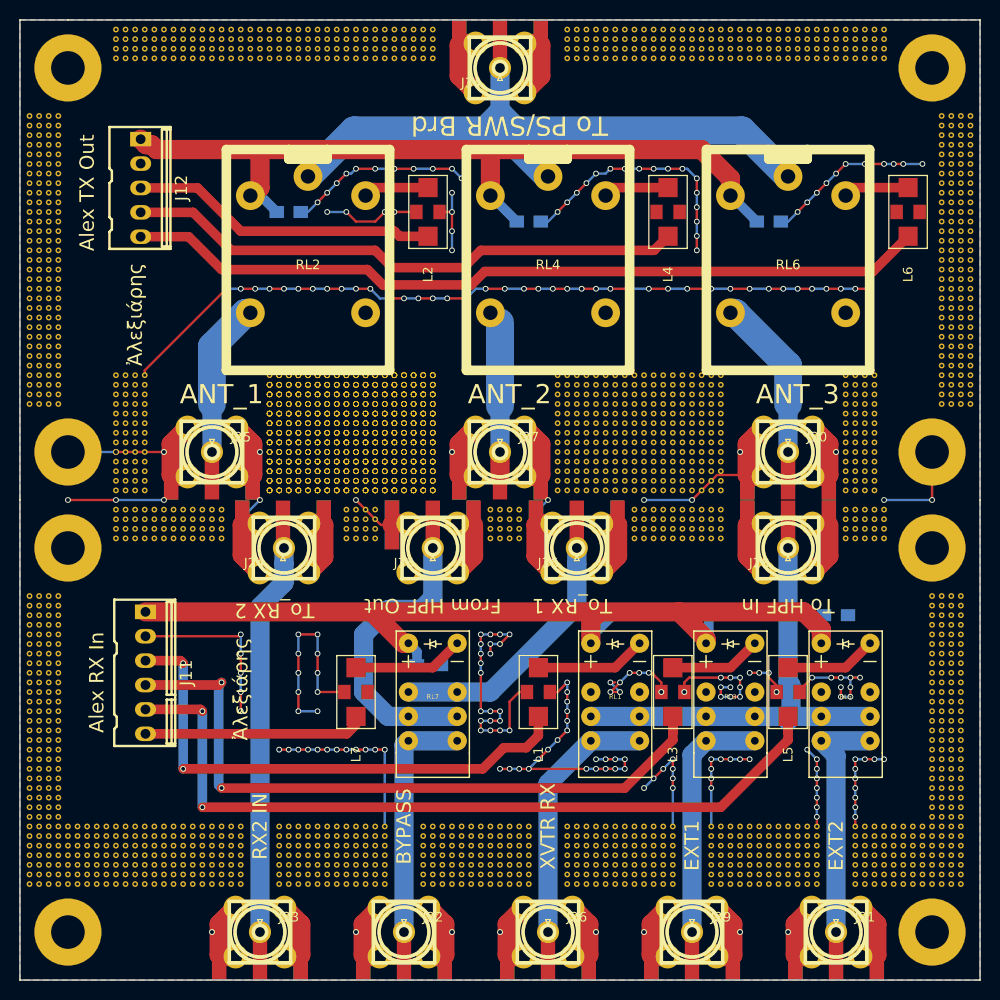
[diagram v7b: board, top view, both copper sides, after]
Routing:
- net GND: track 540.4 -> 690.0 mm, vias 86 -> 247
